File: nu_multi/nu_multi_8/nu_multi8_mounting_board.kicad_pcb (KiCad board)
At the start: 2 copper layers, 95.2 x 18.2 mm, 18 parts, among them J1 CONN_01X03, J10 CONN_01X03, J11 CONN_01X02, J12 CONN_01X03, J13 CONN_01X02, J14 CONN_01X03, J15 CONN_01X02, J16 CONN_01X03, J17 CONN_01X14, J2 CONN_01X02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

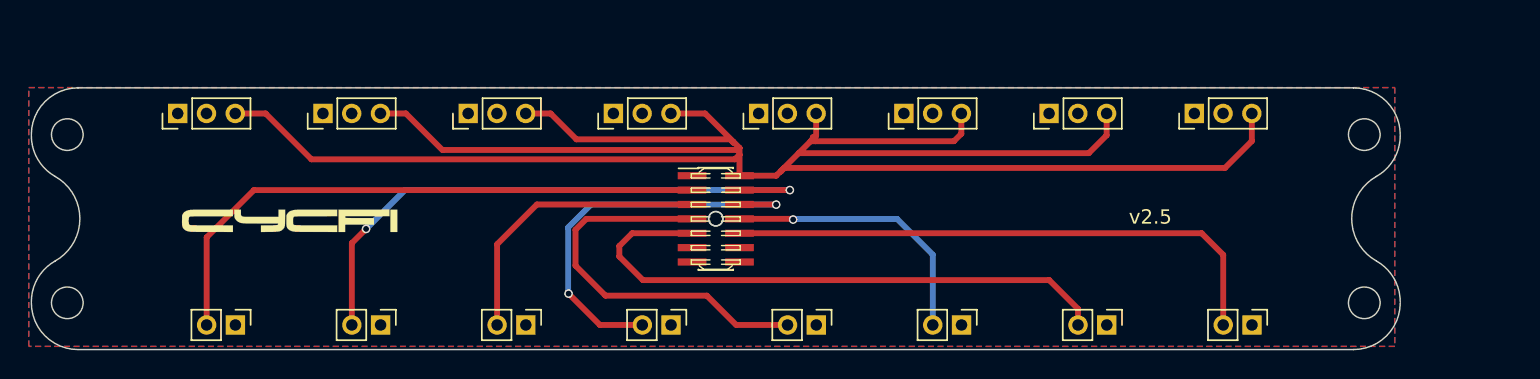
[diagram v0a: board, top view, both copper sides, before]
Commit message: - Fix wrong string spacing - Bump version to v2.54
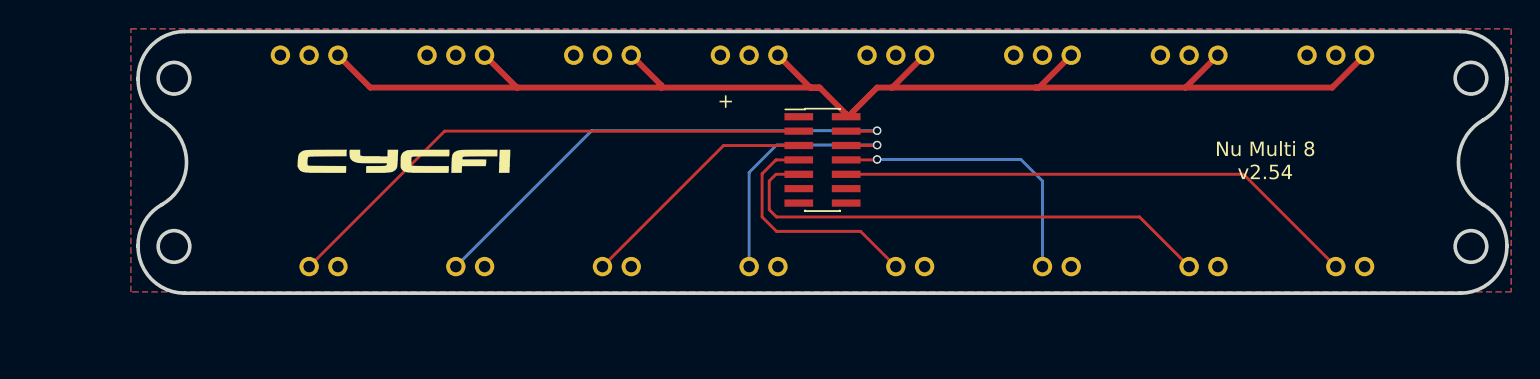
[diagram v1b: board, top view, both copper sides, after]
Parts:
- removed the G*** at (112.2, 95.2)
- removed J1, J10, J12, J14, J16, J6, J7, J8: CONN_01X03, Pin_Headers:Pin_Header_Straight_1x03_Pitch2.00mm
- removed J11, J15, J2, J3, J4, J5, J9: CONN_01X02, Pin_Headers:Pin_Header_Straight_1x02_Pitch2.00mm
- removed J17: CONN_01X14, Pin_Headers:Pin_Header_Straight_2x07_Pitch1.00mm_SMD
- added G***: LOGO, cycfi_library:cycfi-logo-15mm, F.Cu at (120.0, 91.2)
- added U1: nu_capsule, cycfi_library:nu_capsule, F.Cu at (111.5, 83.8)
- added U2: nu_capsule, cycfi_library:nu_capsule, F.Cu at (121.7, 83.8)
- added U3: nu_capsule, cycfi_library:nu_capsule, F.Cu at (131.9, 83.8)
- added U4: nu_capsule, cycfi_library:nu_capsule, F.Cu at (142.1, 83.8)
- added U5: nu_capsule, cycfi_library:nu_capsule, F.Cu at (152.3, 83.8)
- added U6: nu_capsule, cycfi_library:nu_capsule, F.Cu at (162.5, 83.8)
- added U7: nu_capsule, cycfi_library:nu_capsule, F.Cu at (172.7, 83.8)
- added U8: nu_capsule, cycfi_library:nu_capsule, F.Cu at (182.9, 83.8)
- J13: value CONN_01X02 -> CONN_01X14; footprint Pin_Headers:Pin_Header_Straight_1x02_Pitch2.00mm -> cycfi_library:pin_header_2x7p_1.00mm_smd_vertical
- moved J13 32.8 mm to (149.2, 91.0), turned to 0 degrees
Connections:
- J13 pad 2: Net-(J13-Pad2) -> V+
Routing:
- net V+: track 165.3 -> 95.1 mm
- net Net-(J15-Pad2): track 41.2 -> 0.00 mm
- net Net-(J13-Pad2): track 41.2 -> 0.00 mm, vias 2 -> 0
- net Net-(J17-Pad9): track 40.7 -> 0.00 mm
- net Net-(J17-Pad10): track 39.1 -> 0.00 mm
- net CH1: track 0.00 -> 38.0 mm
- net CH8: track 0.00 -> 36.7 mm
- net CH2: track 0.00 -> 35.4 mm, vias 0 -> 1
- net CH7: track 0.00 -> 35.1 mm
- net Net-(J17-Pad6): track 28.3 -> 0.00 mm, vias 2 -> 0
- net Net-(J17-Pad7): track 27.4 -> 0.00 mm
- net Net-(J11-Pad2): track 20.3 -> 0.00 mm
- net CH6: track 0.00 -> 20.2 mm, vias 0 -> 1
- net Net-(J17-Pad8): track 19.4 -> 0.00 mm, vias 1 -> 0
- net CH4: track 0.00 -> 18.4 mm, vias 0 -> 1
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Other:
- outline, holes or cut-outs redrawn
- net class Default removed
- board text added: "+"
- board text added: "Nu Multi 8 v2.54"
- board text removed: "v2.5"
